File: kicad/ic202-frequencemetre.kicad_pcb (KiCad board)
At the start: 2 copper layers, 0 parts

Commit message: Placement initial du PCB (80x70mm, paysage)
Contraintes imposees respectees : J1 (+12V IN) bord haut au milieu,
J2 (RF IN) bord gauche, J4 (nappe LCD) bord droit, A1 (Arduino sur
picots) a droite pres de J4 en paysage avec l'extremite USB/FTDI a
gauche - rotation verifiee par mesure des pads (get_pad_position),
pas deduite du symbole schema.

Reste des 39 empreintes reparti par proximite en respectant les
groupes de la propriete Placement (decouplage LOCAL, boucles LOOP
CRITIQUE RF et chemin de comptage). 0 chevauchement de courtyard,
0 erreur DRC (1 avertissement cosmetique silkscreen).

Nouveau skill Claude Code kicad-pcb-placement documentant la
methode (contraintes dures verifiees par outil, brouillon de
placement valide via check_courtyard_overlaps avant tout
deplacement reel, verification empirique de l'orientation des
empreintes montees sur picots).

Co-Authored-By: Claude Sonnet 5 <noreply@anthropic.com>
Claude-Session: https://claude.ai/code/session_017jkpXZgM5sH1vt8JFfAijf
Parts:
- added A1: Pro Mini 3V3/8MHz, frequencemetre:Arduino_Pro_Mini_Header_2x12, F.Cu at (50.0, 41.0)
- added C1: 100n, Capacitor_SMD:C_0603_1608Metric, F.Cu at (12.0, 20.0)
- added C10: 100n, Capacitor_SMD:C_0603_1608Metric, F.Cu at (36.0, 64.0)
- added C11: 100n, Capacitor_SMD:C_0603_1608Metric, F.Cu at (60.0, 58.0)
- added C12: 1u, Capacitor_SMD:C_0805_2012Metric, F.Cu at (74.0, 60.0)
- added C2: 10u, Capacitor_SMD:C_0805_2012Metric, F.Cu at (12.0, 28.0)
- added C3: 100n, Capacitor_SMD:C_0603_1608Metric, F.Cu at (34.0, 20.0)
- added C4: 10u, Capacitor_SMD:C_0805_2012Metric, F.Cu at (34.0, 28.0)
- added C5: 100n, Capacitor_SMD:C_0603_1608Metric, F.Cu at (62.0, 20.0)
- added C6: 10u, Capacitor_SMD:C_0805_2012Metric, F.Cu at (62.0, 28.0)
- added C7: 1n, Capacitor_SMD:C_0603_1608Metric, F.Cu at (14.0, 44.0)
- added C8: 100n, Capacitor_SMD:C_0603_1608Metric, F.Cu at (14.0, 52.0)
- added C9: 100n, Capacitor_SMD:C_0603_1608Metric, F.Cu at (24.0, 54.0)
- added J1: +12V IN, Connector_PinHeader_2.54mm:PinHeader_1x02_P2.54mm_Vertical, F.Cu at (40.0, 6.00)
- added J2: RF IN, TestPoint:TestPoint_2Pads_Pitch2.54mm_Drill0.8mm, F.Cu at (6.00, 42.0)
- added J4: LCD, Connector_PinHeader_2.54mm:PinHeader_1x10_P2.54mm_Vertical, F.Cu at (76.0, 30.0)
- added Q1: 2N2369, Package_TO_SOT_THT:TO-92_Inline, F.Cu at (52.0, 58.0)
- added R1: 220R, Resistor_SMD:R_0603_1608Metric, F.Cu at (70.0, 20.0)
- added R10: 100k, Resistor_SMD:R_0603_1608Metric, F.Cu at (70.0, 49.0)
- added R11: 100k, Resistor_SMD:R_0603_1608Metric, F.Cu at (70.0, 54.0)
- added R12: 100k, Resistor_SMD:R_0603_1608Metric, F.Cu at (70.0, 59.0)
- added R13: 100k, Resistor_SMD:R_0603_1608Metric, F.Cu at (70.0, 64.0)
- added R14: 100k, Resistor_SMD:R_0603_1608Metric, F.Cu at (70.0, 68.5)
- added R15: 100k, Resistor_SMD:R_0603_1608Metric, F.Cu at (65.0, 52.0)
- added R16: 100k, Resistor_SMD:R_0603_1608Metric, F.Cu at (65.0, 57.0)
- added R17: 3k3, Resistor_SMD:R_0603_1608Metric, F.Cu at (65.0, 62.0)
- added R18: 3k3, Resistor_SMD:R_0603_1608Metric, F.Cu at (65.0, 67.0)
- added R19: 2K2, Resistor_SMD:R_0603_1608Metric, F.Cu at (36.0, 56.0)
- added R2: 300R, Resistor_SMD:R_0603_1608Metric, F.Cu at (70.0, 28.0)
- added R20: 470K, Resistor_SMD:R_0603_1608Metric, F.Cu at (14.0, 60.0)
- added R3: 51R, Resistor_SMD:R_0603_1608Metric, F.Cu at (14.0, 36.0)
- added R4: 3k3, Resistor_SMD:R_0603_1608Metric, F.Cu at (44.0, 56.0)
- added R6: 470R, Resistor_SMD:R_0603_1608Metric, F.Cu at (44.0, 64.0)
- added R7: 100k, Resistor_SMD:R_0603_1608Metric, F.Cu at (70.0, 34.0)
- added R8: 100k, Resistor_SMD:R_0603_1608Metric, F.Cu at (70.0, 39.0)
- added R9: 100k, Resistor_SMD:R_0603_1608Metric, F.Cu at (70.0, 44.0)
- added U1: AMS1117-5.0, Package_TO_SOT_SMD:SOT-223-3_TabPin2, F.Cu at (22.0, 20.0)
- added U2: AMS1117 (ADJ), Package_TO_SOT_SMD:SOT-223-3_TabPin2, F.Cu at (52.0, 20.0)
- added U3: MB506, Package_DIP:DIP-8_W7.62mm, F.Cu at (24.0, 42.0)
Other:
- board outline added: 80 x 70 mm

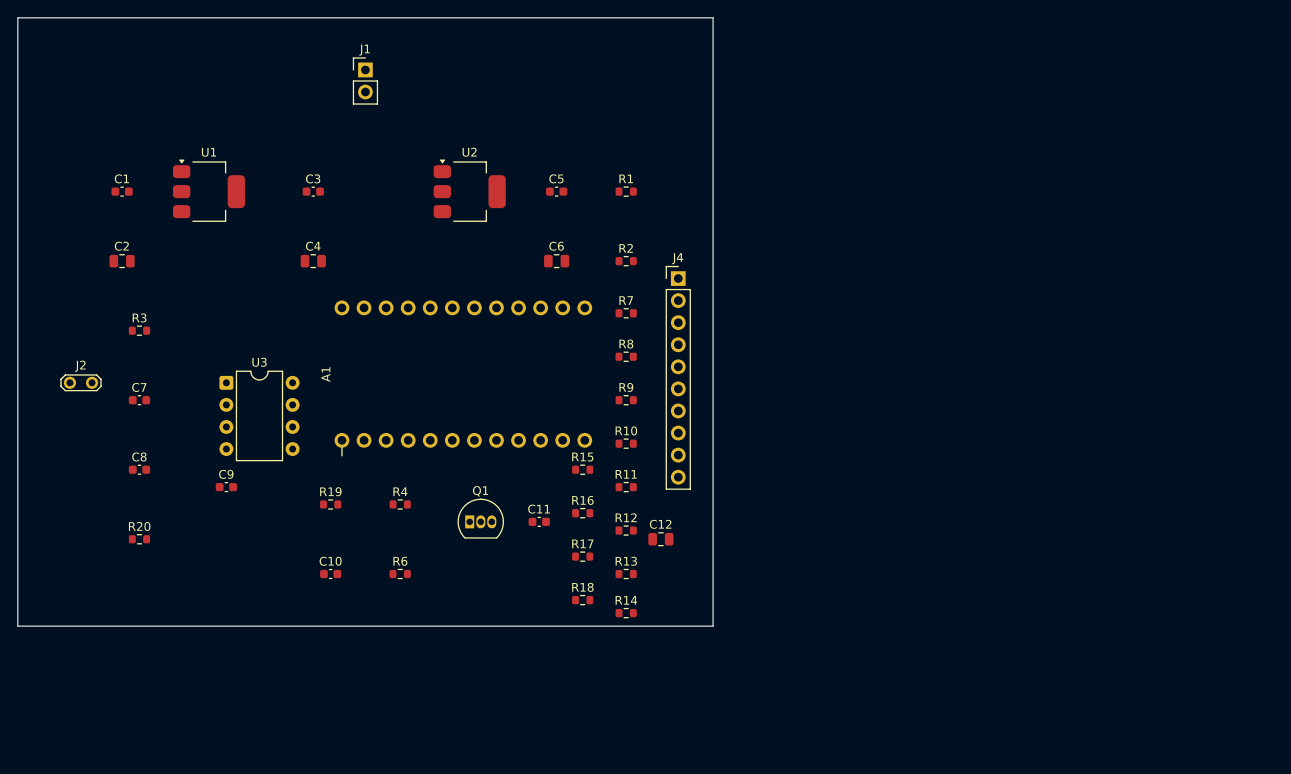
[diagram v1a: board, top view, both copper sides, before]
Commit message: U3->SOP-8, Q1->SOT-89, J1->4 broches ; cavaliers devant J4 ; replacement 80x50mm
Schema :
- U3 (MB506) : DIP-8 -> SOP-8 (MB506PF Fujitsu, stock PartsBox), meme
  brochage 1-8, pas de changement de symbole.
- Q1 : 2N2369 (TO-18) -> 2SC5551AE-TD-E (onsemi, SOT-89, fT=3.5GHz, stock
  PartsBox). Symbole remplace par Q_NPN_BCE (meme geometrie de broches que
  Q_NPN_BEC, seul l'etiquetage broche/fonction change) pour correspondre au
  brochage reel du SOT-89 (broche 2 = collecteur sur la languette).
- J1 : connecteur 2 broches -> 4 broches, paires adjacentes 1-2=+12V et
  3-4=GND. Corrige au passage un bug preexistant (les 2 broches d'origine
  et leurs labels +12V/GND etaient orphelins, non relies par un fil).
- 10 cavaliers a souder JP1-JP10 (Jumper:SolderJumper_2_Open, ouverts par
  defaut) inseres en serie entre R7-R16 et chaque broche de J4, pour
  pouvoir isoler la carte de la nappe LCD.

PCB :
- Board reduit de 80x70mm a 80x50mm.
- Nouveau placement complet : A1 decale de 3mm vers la gauche, R7-R16
  places dans le volume libre sous A1 (entre les deux barrettes de picots),
  reste reparti par proximite. 0 erreur run_drc (kicad-cli), 3
  avertissements silkscreen cosmetiques.
- Limitation d'outil documentee (README + skill kicad-pcb-placement) :
  check_courtyard_overlaps (MCP) juge sur la bounding box globale d'une
  empreinte, pas ses polygones reels - faux positifs sur les empreintes a
  courtyards multiples comme celle de A1. run_drc fait foi.

Co-Authored-By: Claude Sonnet 5 <noreply@anthropic.com>
Claude-Session: https://claude.ai/code/session_017jkpXZgM5sH1vt8JFfAijf
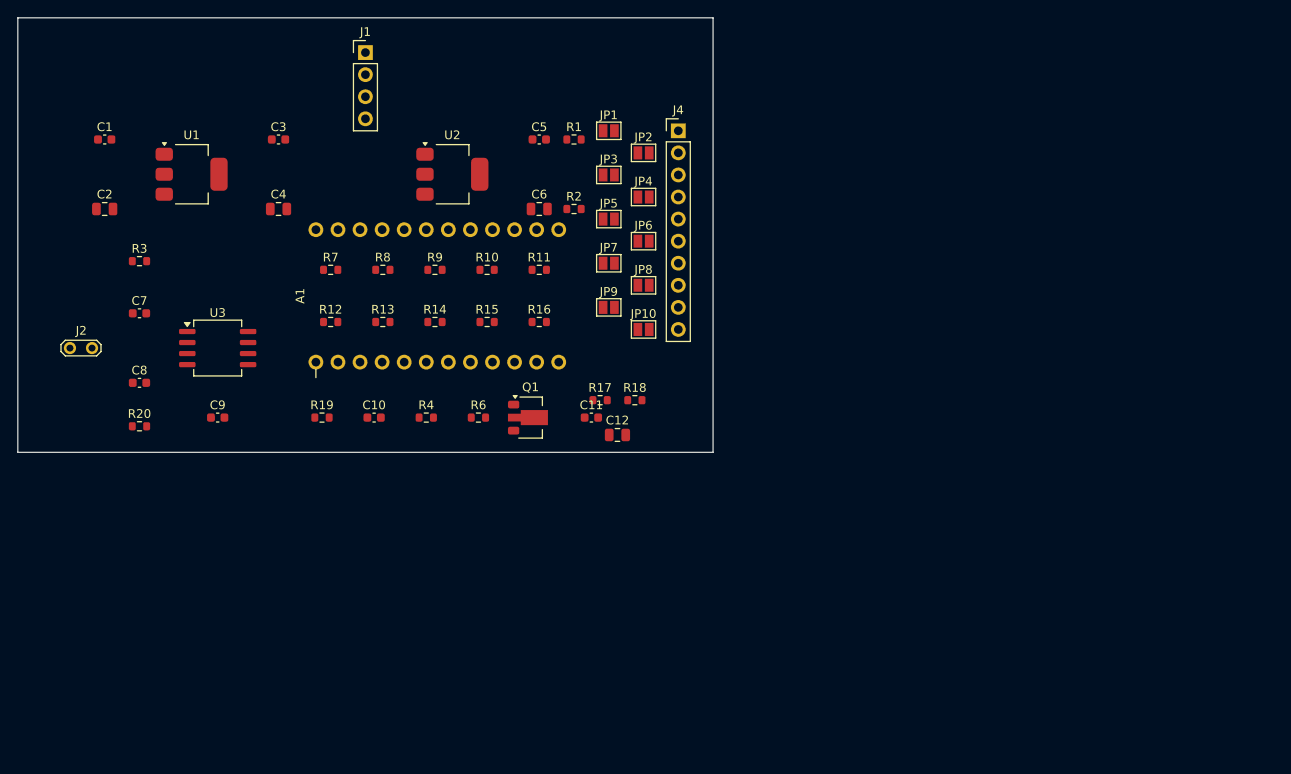
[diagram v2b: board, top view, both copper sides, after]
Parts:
- added JP1: SolderJumper_2_Open, Jumper:SolderJumper-2_P1.3mm_Open_Pad1.0x1.5mm, F.Cu at (68.0, 13.0)
- added JP10: SolderJumper_2_Open, Jumper:SolderJumper-2_P1.3mm_Open_Pad1.0x1.5mm, F.Cu at (72.0, 35.9)
- added JP2: SolderJumper_2_Open, Jumper:SolderJumper-2_P1.3mm_Open_Pad1.0x1.5mm, F.Cu at (72.0, 15.5)
- added JP3: SolderJumper_2_Open, Jumper:SolderJumper-2_P1.3mm_Open_Pad1.0x1.5mm, F.Cu at (68.0, 18.1)
- added JP4: SolderJumper_2_Open, Jumper:SolderJumper-2_P1.3mm_Open_Pad1.0x1.5mm, F.Cu at (72.0, 20.6)
- added JP5: SolderJumper_2_Open, Jumper:SolderJumper-2_P1.3mm_Open_Pad1.0x1.5mm, F.Cu at (68.0, 23.2)
- added JP6: SolderJumper_2_Open, Jumper:SolderJumper-2_P1.3mm_Open_Pad1.0x1.5mm, F.Cu at (72.0, 25.7)
- added JP7: SolderJumper_2_Open, Jumper:SolderJumper-2_P1.3mm_Open_Pad1.0x1.5mm, F.Cu at (68.0, 28.2)
- added JP8: SolderJumper_2_Open, Jumper:SolderJumper-2_P1.3mm_Open_Pad1.0x1.5mm, F.Cu at (72.0, 30.8)
- added JP9: SolderJumper_2_Open, Jumper:SolderJumper-2_P1.3mm_Open_Pad1.0x1.5mm, F.Cu at (68.0, 33.3)
- J1: value +12V IN -> +12V IN (4 pins: 2x+12V, 2x GND); footprint Connector_PinHeader_2.54mm:PinHeader_1x02_P2.54mm_Vertical -> Connector_PinHeader_2.54mm:PinHeader_1x04_P2.54mm_Vertical
- Q1: value 2N2369 -> 2SC5551AE-TD-E; footprint Package_TO_SOT_THT:TO-92_Inline -> Package_TO_SOT_SMD:SOT-89-3
- U3: footprint Package_DIP:DIP-8_W7.62mm -> Package_SO:SOIC-8_5.3x6.2mm_P1.27mm
- moved R12 41.6 mm to (36.0, 35.0)
- moved R13 40.3 mm to (42.0, 35.0)
- moved R14 40.1 mm to (48.0, 35.0)
- moved R7 34.4 mm to (36.0, 29.0)
- moved R8 29.7 mm to (42.0, 29.0)
- moved R11 26.9 mm to (60.0, 29.0)
- moved R9 26.6 mm to (48.0, 29.0)
- moved R10 25.6 mm to (54.0, 29.0)
- moved R18 23.8 mm to (71.0, 44.0)
- moved R16 22.6 mm to (60.0, 35.0)
- moved R15 20.2 mm to (54.0, 35.0)
- moved R6 20.1 mm to (53.0, 46.0)
- moved C10 18.7 mm to (41.0, 46.0)
- moved R17 18.1 mm to (67.0, 44.0)
- moved J4 17.0 mm to (76.0, 13.0)
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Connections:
- J1 pad 2: GND -> +12V
- Q1 pad 2: GND -> D5_SIG
- Q1 pad 3: D5_SIG -> GND
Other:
- board size 80 x 70 mm -> 80 x 50 mm

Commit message: J1/J2 : broches paralleles au bord le plus proche (regle par defaut)
J1 (header 1x04, bord haut) et J2 (2 pastilles, bord gauche) avaient leurs
broches perpendiculaires au bord le plus proche (orientation par defaut du
footprint, non revue). Tourne a 90 degres chacun pour aligner la rangee de
broches parallelement au bord ; J1 repositionne en x pour eviter U1/U2 une
fois sa courtyard devenue plus large que haute. 0 erreur run_drc, 0
chevauchement courtyard (hors faux positifs connus sur A1).

Nouvelle regle par defaut ajoutee au skill kicad-pcb-placement : un
connecteur pres d'un bord se place broches paralleles a ce bord, sauf
orientation contraire explicitement demandee.

Co-Authored-By: Claude Sonnet 5 <noreply@anthropic.com>
Claude-Session: https://claude.ai/code/session_017jkpXZgM5sH1vt8JFfAijf
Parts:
- moved J1 9.00 mm to (31.0, 4.00), turned to 90 degrees
- turned J2 to 90 degrees
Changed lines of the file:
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@@
 	(footprint "Connector_PinHeader_2.54mm:PinHeader_1x04_P2.54mm_Vertical"
 		(layer "F.Cu")
-		(at 40 4)
+		(at 31 4 90)
 		(descr "Through hole straight pin header, 1x04, 2.54mm pitch, single row")
 		(tags "Through hole pin header THT 1x04 2.54mm single row")
 		(property "Reference" "J1"
-			(at 0 -2.38 0)
+			(at 0 -2.38 90)
 			(layer "F.SilkS")
 			(effects
@@
 		)
 		(property "Value" "+12V IN (4 pins: 2x+12V, 2x GND)"
-			(at 0 10 0)
+			(at 0 10 90)
 			(layer "F.Fab")
 			(effects
@@
 		)
 		(property "Datasheet" ""
-			(at 0 0 0)
+			(at 0 0 90)
 			(layer "F.Fab")
 			(hide yes)
@@
 		)
 		(property "Description" ""
-			(at 0 0 0)
+			(at 0 0 90)
 			(layer "F.Fab")
 			(hide yes)
@@
 		)
 		(property "KiLib_Generator" "connector/pin_header_socket"
-			(at 0 0 0)
+			(at 0 0 90)
 			(layer "F.SilkS")
 			(hide yes)
@@
 		)
 		(fp_line
-			(start -1.38 1.27)
-			(end -1.38 9)
+			(start 1.38 1.27)
+			(end 1.38 9)
 			(stroke
 				(width 0.12)
@@
 		)
 		(fp_line
-			(start -1.38 9)
-			(end 1.38 9)
+			(start -1.38 1.27)
+			(end -1.38 9)
 			(stroke
 				(width 0.12)
@@
 		)
 		(fp_line
-			(start 1.38 1.27)
+			(start -1.38 9)
 			(end 1.38 9)
 			(stroke
@@
 		)
 		(fp_line
-			(start -1.27 -0.635)
-			(end -0.635 -1.27)
+			(start 1.27 -1.27)
+			(end 1.27 8.89)
 			(stroke
 				(width 0.1)
@@
 		)
 		(fp_line
-			(start -1.27 8.89)
-			(end -1.27 -0.635)
+			(start -0.635 -1.27)
+			(end 1.27 -1.27)
 			(stroke
 				(width 0.1)
@@
 		)
 		(fp_line
-			(start -0.635 -1.27)
-			(end 1.27 -1.27)
+			(start -1.27 -0.635)
+			(end -0.635 -1.27)
 			(stroke
 				(width 0.1)
@@
 		)
 		(fp_line
-			(start 1.27 -1.27)
-			(end 1.27 8.89)
+			(start 1.27 8.89)
+			(end -1.27 8.89)
 			(stroke
 				(width 0.1)
@@
 		)
 		(fp_line
-			(start 1.27 8.89)
-			(end -1.27 8.89)
+			(start -1.27 8.89)
+			(end -1.27 -0.635)
 			(stroke
 				(width 0.1)
@@
 		)
 		(fp_text user "${REFERENCE}"
-			(at 0 3.81 90)
+			(at 0 3.81 180)
 			(layer "F.Fab")
 			(effects
@@
 		)
 		(pad "1" thru_hole rect
-			(at 0 0)
+			(at 0 0 90)
 			(size 1.7 1.7)
 			(drill 1)
@@
 		)
 		(pad "2" thru_hole circle
-			(at 0 2.54)
+			(at 0 2.54 90)
 			(size 1.7 1.7)
 			(drill 1)
@@
 		)
 		(pad "3" thru_hole circle
-			(at 0 5.08)
+			(at 0 5.08 90)
 			(size 1.7 1.7)
 			(drill 1)
@@
 		)
 		(pad "4" thru_hole circle
-			(at 0 7.62)
+			(at 0 7.62 90)
 			(size 1.7 1.7)
 			(drill 1)
@@
 	(footprint "TestPoint:TestPoint_2Pads_Pitch2.54mm_Drill0.8mm"
 		(layer "F.Cu")
-		(at 6 38)
+		(at 6 38 90)
 		(descr "Test point with 2 pins, pitch 2.54mm, drill diameter 0.8mm")
 		(tags "CONN DEV")
 		(property "Reference" "J2"
-			(at 1.3 -2 0)
+			(at 1.3 -2 90)
 			(layer "F.SilkS")
 			(effects
@@
 		)
 		(property "Value" "RF IN"
-			(at 1.27 2 0)
+			(at 1.27 2 90)
 			(layer "F.Fab")
 			(effects
@@
 		)
 		(property "Datasheet" ""
-			(at 0 0 0)
+			(at 0 0 90)
 			(unlocked yes)
 			(layer "F.Fab")
@@
 		)
 		(property "Description" ""
-			(at 0 0 0)
+			(at 0 0 90)
 			(unlocked yes)
 			(layer "F.Fab")
@@
 		(duplicate_pad_numbers_are_jumpers no)
 		(fp_line
-			(start -1.03 -0.4)
-			(end -0.53 -0.9)
+			(start 3.07 -0.9)
+			(end 3.57 -0.4)
 			(stroke
 				(width 0.15)
@@
 		)
 		(fp_line
-			(start -1.03 0.4)
-			(end -1.03 -0.4)
+			(start -0.53 -0.9)
+			(end 3.07 -0.9)
 			(stroke
 				(width 0.15)
@@
 		)
 		(fp_line
-			(start -0.53 -0.9)
-			(end 3.07 -0.9)
+			(start 3.57 -0.4)
+			(end 3.57 0.4)
 			(stroke
 				(width 0.15)
@@
 		)
 		(fp_line
-			(start -0.53 0.9)
-			(end -1.03 0.4)
+			(start -1.03 -0.4)
+			(end -0.53 -0.9)
 			(stroke
 				(width 0.15)
@@
 		)
 		(fp_line
-			(start 3.07 -0.9)
-			(end 3.57 -0.4)
+			(start 3.57 0.4)
+			(end 3.07 0.9)
 			(stroke
 				(width 0.15)
@@
 		)
 		(fp_line
-			(start 3.07 0.9)
-			(end -0.53 0.9)
+			(start -1.03 0.4)
+			(end -1.03 -0.4)
 			(stroke
 				(width 0.15)
@@
 		)
 		(fp_line
-			(start 3.57 -0.4)
-			(end 3.57 0.4)
+			(start 3.07 0.9)
+			(end -0.53 0.9)
 			(stroke
 				(width 0.15)
@@
 		)
 		(fp_line
-			(start 3.57 0.4)
-			(end 3.07 0.9)
+			(start -0.53 0.9)
+			(end -1.03 0.4)
 			(stroke
 				(width 0.15)
@@
 		)
 		(fp_line
-			(start -1.3 -0.5)
-			(end -1.3 0.5)
+			(start 3.15 -1.15)
+			(end -0.65 -1.15)
 			(stroke
 				(width 0.05)
@@
 		)
 		(fp_line
-			(start -1.3 0.5)
-			(end -0.65 1.15)
+			(start -0.65 -1.15)
+			(end -1.3 -0.5)
 			(stroke
 				(width 0.05)
@@
 		)
 		(fp_line
-			(start -0.65 -1.15)
-			(end -1.3 -0.5)
+			(start 3.8 -0.5)
+			(end 3.15 -1.15)
 			(stroke
 				(width 0.05)
@@
 		)
 		(fp_line
-			(start -0.65 1.15)
-			(end 3.15 1.15)
+			(start -1.3 -0.5)
+			(end -1.3 0.5)
 			(stroke
 				(width 0.05)
@@
 		)
 		(fp_line
-			(start 3.15 -1.15)
-			(end -0.65 -1.15)
+			(start 3.8 0.5)
+			(end 3.8 -0.5)
 			(stroke
 				(width 0.05)
@@
 		)
 		(fp_line
-			(start 3.15 1.15)
-			(end 3.8 0.5)
+			(start -1.3 0.5)
+			(end -0.65 1.15)
 			(stroke
 				(width 0.05)
@@
 		)
 		(fp_line
-			(start 3.8 -0.5)
-			(end 3.15 -1.15)
+			(start 3.15 1.15)
+			(end 3.8 0.5)
 			(stroke
 				(width 0.05)
@@
 		)
 		(fp_line
-			(start 3.8 0.5)
-			(end 3.8 -0.5)
+			(start -0.65 1.15)
+			(end 3.15 1.15)
 			(stroke
 				(width 0.05)
@@
 		)
 		(fp_text user "${REFERENCE}"
-			(at 1.3 -2 0)
+			(at 1.3 -2 90)
 			(layer "F.Fab")
 			(effects
@@
 		)
 		(pad "1" thru_hole circle
-			(at 0 0)
+			(at 0 0 90)
 			(size 1.4 1.4)
 			(drill 0.8)
@@
 		)
 		(pad "2" thru_hole circle
-			(at 2.54 0)
+			(at 2.54 0 90)
 			(size 1.4 1.4)
 			(drill 0.8)

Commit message: Corrige un court-circuit entre lignes LCD introduit par le routage des cavaliers
Les 10 fils cavalier->J4 passaient par un coude a abscisse commune
(x=330.2). Les pas differents cote resistances (5,08mm) et cote J4
(2,54mm) faisaient que plusieurs segments verticaux se chevauchaient sur
cette abscisse, court-circuitant COM2-COM3-COM4-SEG1 d'un cote et
SEG3-SEG4 de l'autre. Trouve en tentant un premier routage (l'ERC ne
signalait qu'un avertissement discret, pas une erreur).

Corrige : les 10 chemins coudes remplaces par un fil diagonal unique par
ligne (aucun point partage entre lignes differentes). Chaque broche de J4
recoit aussi un label explicite (J4_COM1..J4_SEG6) : sync_schematic_to_board
echouait silencieusement a resoudre les nets anonymes auto-generes par
KiCad, laissant ces broches sans net cote PCB.

Verifie via kicad-cli sch export netlist (parse par comptage de
parentheses, pas de grep naif) : chaque ligne LCD forme maintenant
exactement 2 nets distincts et corrects. ERC : 0 erreur (3 avertissements
label_multiple_wires cosmetiques). run_drc PCB : 0 erreur.

Pieges documentes dans le skill kicad (nets anonymes non resolus par
sync_schematic_to_board, chevauchement de coudes de routage a pas
differents, necessite de parser le netlist par comptage de parentheses).

Co-Authored-By: Claude Sonnet 5 <noreply@anthropic.com>
Claude-Session: https://claude.ai/code/session_017jkpXZgM5sH1vt8JFfAijf
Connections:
- J4 pad 1: LCD_COM1 -> J4_COM1
- J4 pad 10: LCD_SEG6 -> J4_SEG6
- J4 pad 2: LCD_COM2 -> J4_COM2
- J4 pad 3: LCD_COM3 -> J4_COM3
- J4 pad 4: LCD_COM4 -> J4_COM4
- J4 pad 5: LCD_SEG1 -> J4_SEG1
- J4 pad 6: LCD_SEG2 -> J4_SEG2
- J4 pad 7: LCD_SEG3 -> J4_SEG3
- J4 pad 8: LCD_SEG4 -> J4_SEG4
- J4 pad 9: LCD_SEG5 -> J4_SEG5
- JP1 pad 2: (no net) -> J4_COM1
- JP10 pad 2: (no net) -> J4_SEG6
- JP2 pad 2: (no net) -> J4_COM2
- JP3 pad 2: (no net) -> J4_COM3
- JP4 pad 2: (no net) -> J4_COM4
- JP5 pad 2: (no net) -> J4_SEG1
- JP6 pad 2: (no net) -> J4_SEG2
- JP7 pad 2: (no net) -> J4_SEG3
- JP8 pad 2: (no net) -> J4_SEG4
- JP9 pad 2: (no net) -> J4_SEG5
